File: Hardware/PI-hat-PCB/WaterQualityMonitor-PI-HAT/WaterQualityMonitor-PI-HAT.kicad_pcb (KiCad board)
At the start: 2 copper layers, 99.1 x 99.7 mm, 90 parts, among them IC1 P82B96TD,118, IC2 DMMT5401-7-F, J1 Screw_Terminal_01x04, J10 GPIO, J2 Screw_Terminal_01x04, J3 Screw_Terminal_01x04, J4 Screw_Terminal_01x02, J5 Jack-DC 12V+, J6 SM04B-SRSS-TB(LF)(SN), J7 Screw_Terminal_01x02, J8 Screw_Terminal_01x02, M1 Fan, Q1 IRL540SPBF, Q2 IRL540SPBF, Q3 DMG2305UX-7, Q4 IRL540SPBF, Q5 IRL540SPBF, U1 DRV8870DDA, U2 TPS61169DCKR, U3 TMC2208_SILENTSTEPSTICK, U4 TMC2208_SILENTSTEPSTICK, U5 RT7272AGSP, U6 TMC2208_SILENTSTEPSTICK, U7 DRV8838, U8 RT7272AGSP, U9 CAT24C256

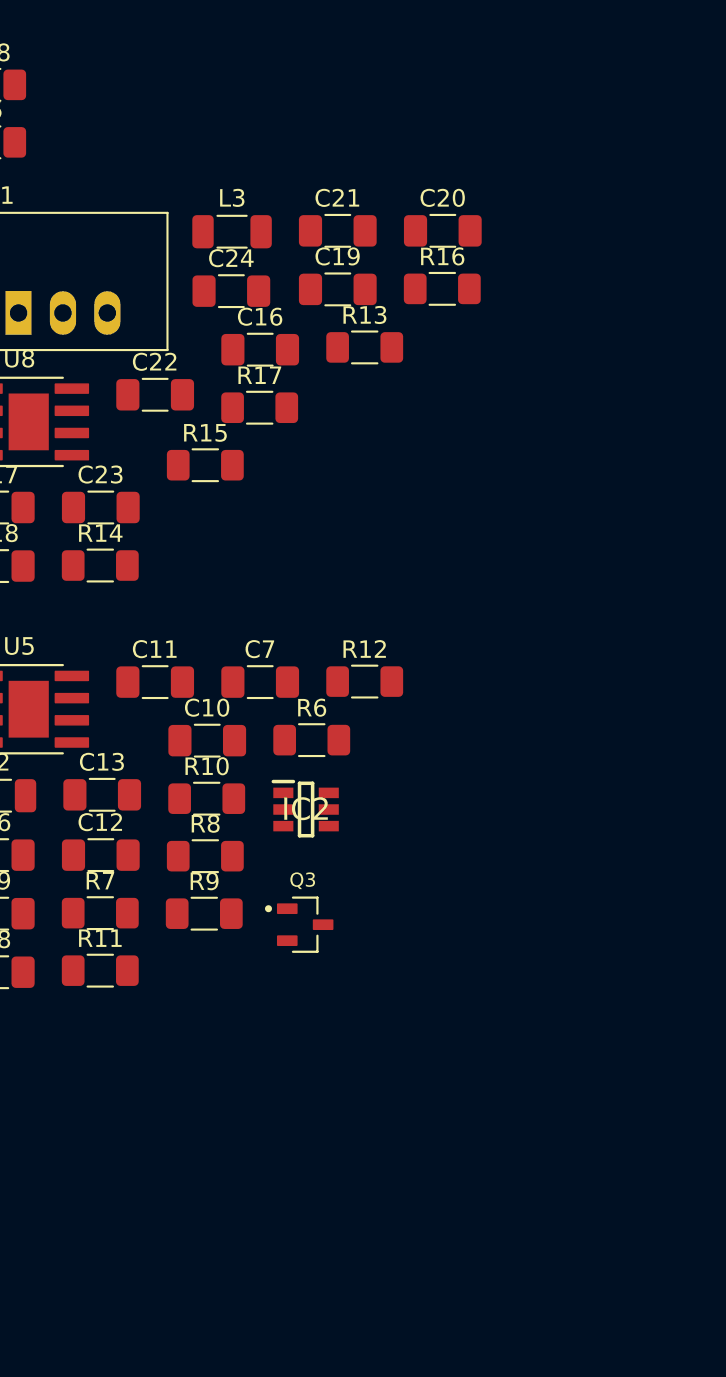
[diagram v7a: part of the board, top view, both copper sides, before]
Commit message: created new bom and experimented with BOM file
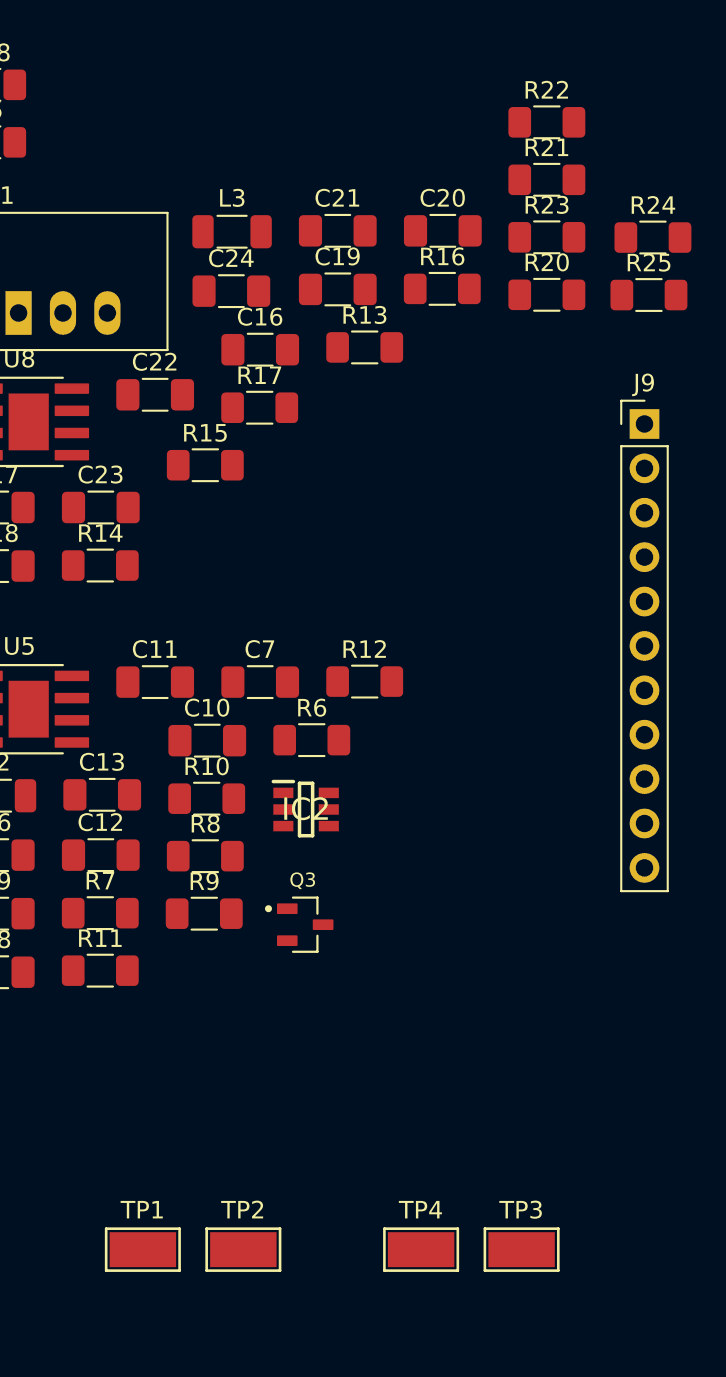
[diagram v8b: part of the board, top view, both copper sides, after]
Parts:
- added J9: Conn_01x11_Male, Connector_PinHeader_2.54mm:PinHeader_1x11_P2.54mm_Vertical, F.Cu at (394.4, 45.1)
- added R20: 22k, Resistor_SMD:R_1206_3216Metric_Pad1.30x1.75mm_HandSolder, F.Cu at (388.8, 37.7)
- added R21: 22k, Resistor_SMD:R_1206_3216Metric_Pad1.30x1.75mm_HandSolder, F.Cu at (388.8, 31.2)
- added R22: 22k, Resistor_SMD:R_1206_3216Metric_Pad1.30x1.75mm_HandSolder, F.Cu at (388.8, 27.9)
- added R23: 22k, Resistor_SMD:R_1206_3216Metric_Pad1.30x1.75mm_HandSolder, F.Cu at (388.8, 34.5)
- added R24: 22k, Resistor_SMD:R_1206_3216Metric_Pad1.30x1.75mm_HandSolder, F.Cu at (394.9, 34.5)
- added R25: 22k, Resistor_SMD:R_1206_3216Metric_Pad1.30x1.75mm_HandSolder, F.Cu at (394.6, 37.8)
- added TP1: TestPoint, TestPoint:TestPoint_Keystone_5019_Minature, F.Cu at (365.7, 92.4)
- added TP2: TestPoint, TestPoint:TestPoint_Keystone_5019_Minature, F.Cu at (371.4, 92.4)
- added TP3: TestPoint, TestPoint:TestPoint_Keystone_5019_Minature, F.Cu at (387.4, 92.4)
- added TP4: TestPoint, TestPoint:TestPoint_Keystone_5019_Minature, F.Cu at (381.6, 92.4)
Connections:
- J10 pad 10: /GPIO[15]/RXD0 -> GPIO15
- J10 pad 11: ENDRV -> PWRGPIO1
- J10 pad 13: PHADRV -> STEPMAIN
- J10 pad 19: /GPIO[10]/SPI0.MOSI -> GPIO10
- J10 pad 21: /GPIO[9]/SPI0.MISO -> GPIO9
- J10 pad 22: /GPIO[25] -> PWRGPIO2
- J10 pad 23: /GPIO[11]/SPI0.SCLK -> GPIO11
- J10 pad 24: /GPIO[8]/SPI0.CE0 -> GPIO8
- J10 pad 26: /GPIO[7]/SPI0.CE1 -> GPIO7
- J10 pad 32: /GPIO[12]/PWM0 -> ENDRV
- J10 pad 33: STEPMAIN -> PHADRV
- J10 pad 36: /GPIO[16] -> GPIO16
- J10 pad 38: /GPIO[20]/PCM.DIN -> GPIO20
- J10 pad 40: /GPIO[21]/PCM.DOUT -> GPIO21
- J10 pad 7: /GPIO[4]/GPCLK0 -> GPIO4
- J10 pad 8: /GPIO[14]/TXD0 -> GPIO14
- Q4 pad 1: CTRLHEAT -> PWRGPIO1
- Q5 pad 1: CTRLHEAT -> PWRGPIO2
- U3 pad JP1_6: unconnected-(U3-PadJP1_6) -> Net-(U3-PadJP1_6)
- U3 pad JP1_7: unconnected-(U3-PadJP1_7) -> Net-(U3-PadJP1_7)
- U4 pad JP1_6: unconnected-(U4-PadJP1_6) -> Net-(U4-PadJP1_6)
- U4 pad JP1_7: unconnected-(U4-PadJP1_7) -> Net-(U4-PadJP1_7)
- U6 pad JP1_6: unconnected-(U6-PadJP1_6) -> Net-(U6-PadJP1_6)
- U6 pad JP1_7: unconnected-(U6-PadJP1_7) -> Net-(U6-PadJP1_7)
